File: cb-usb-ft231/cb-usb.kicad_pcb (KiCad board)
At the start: 2 copper layers, 25.4 x 55.8 mm, 26 parts, among them P1 CONN_01X14, P2 CONN_01X14, P3 CONN_01X05, SW1 SW_PUSH_SMALL, U1 ANTENNA, U2 FT231XS, U3 AP7365-33, U4 LY-SK10

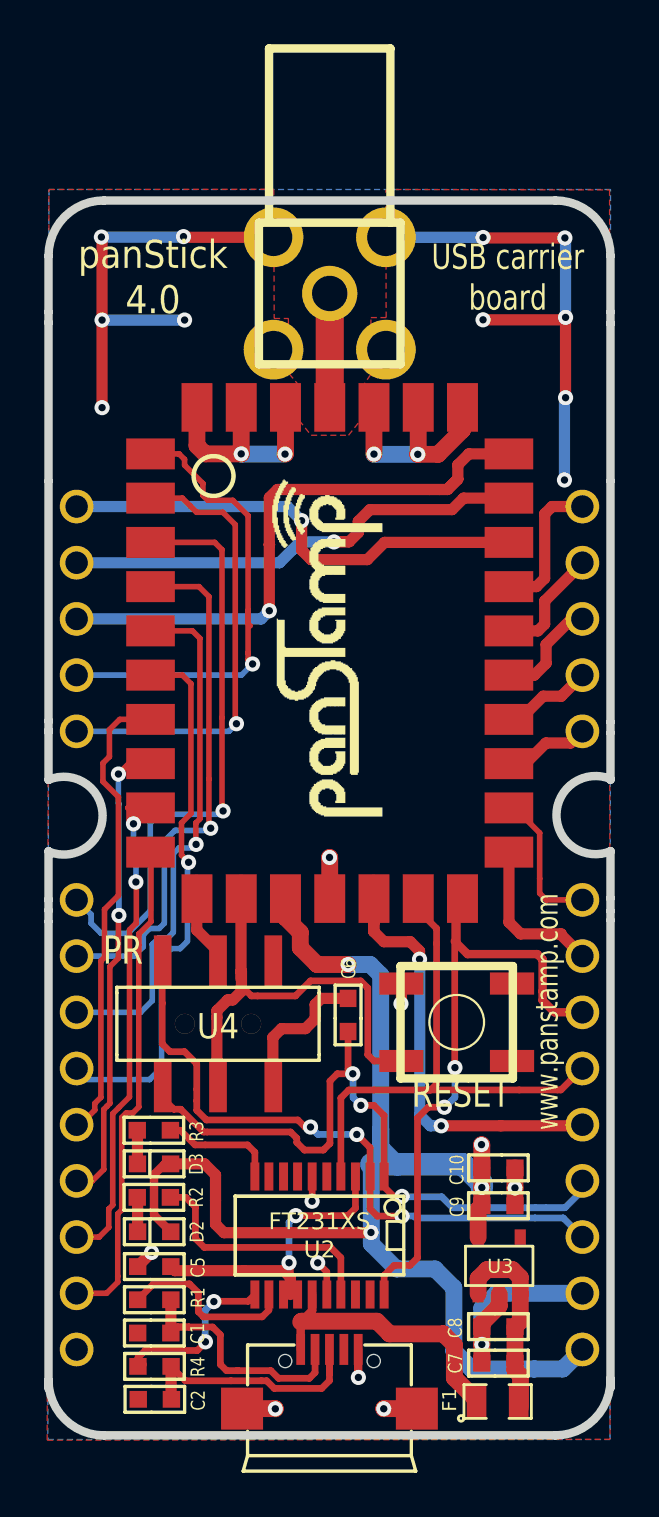
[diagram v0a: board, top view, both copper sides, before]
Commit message: Fiducials added to the PCB
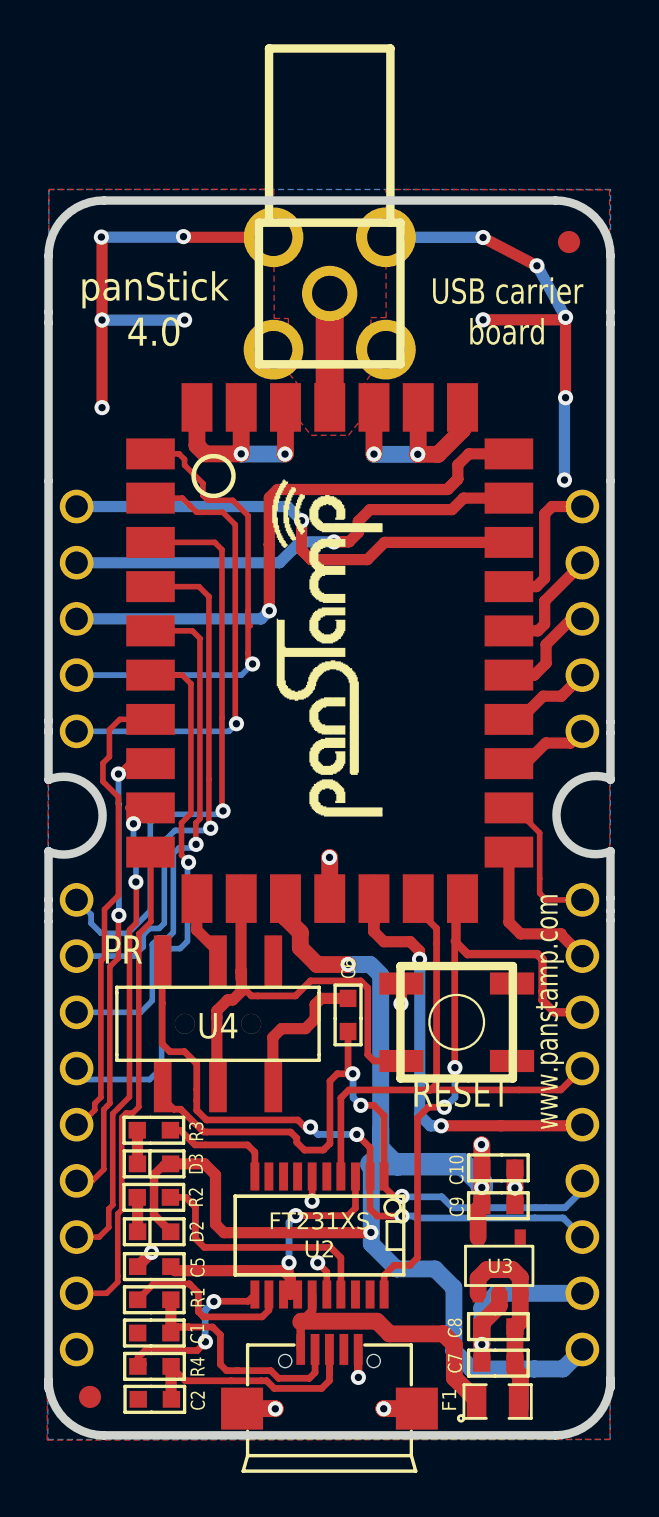
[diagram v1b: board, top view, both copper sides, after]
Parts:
- added fiducial: VAL**, mymods:fiducial, F.Cu at (164.1, 119.8)
- added fiducial: VAL**, mymods:fiducial, F.Cu at (185.8, 67.6)
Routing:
- net GND: track 86.3 -> 84.4 mm
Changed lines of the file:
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@@
-(kicad_pcb (version 4) (host pcbnew "(2014-jul-16 BZR unknown)-product")
+(kicad_pcb (version 4) (host pcbnew no-vcs-found-product)
   (general
     (links 86)
     (no_connects 0)
-    (area 162.059499 65.504799 187.850941 121.703321)
+    (area 154.644817 58.483079 195.375184 125.5577)
     (thickness 1.6002)
     (drawings 70)
     (tracks 695)
     (zones 0)
-    (modules 26)
+    (modules 28)
     (nets 51)
   )
@@
   )
   (setup
-    (last_trace_width 0.381)
+    (last_trace_width 0.1524)
     (user_trace_width 0.2032)
     (user_trace_width 0.254)
@@
     (visible_elements FFFFF7BF)
     (pcbplotparams
-      (layerselection 0x010f0_80000001)
+      (layerselection 0x00020_00000000)
       (usegerberextensions true)
       (excludeedgelayer true)
@@
     )
   )
+  (module mymods:fiducial (layer Front)
+    (at 164.125 119.775)
+    (fp_text reference fiducial (at 0 2.95) (layer F.SilkS) hide
+      (effects (font (thickness 0.3048)))
+    )
+    (fp_text value VAL** (at 0.925 3.625) (layer F.SilkS) hide
+      (effects (font (thickness 0.3048)))
+    )
+    (pad 1 smd circle (at 0 0) (size 1 1) (layers Front F.Mask)
+      (solder_mask_margin 0.5) (clearance 0.5))
+  )
+  (module mymods:fiducial (layer Front)
+    (at 185.775 67.575)
+    (fp_text reference fiducial (at 1.9 -3.65) (layer F.SilkS) hide
+      (effects (font (thickness 0.3048)))
+    )
+    (fp_text value VAL** (at 2.55 -4.1) (layer F.SilkS) hide
+      (effects (font (thickness 0.3048)))
+    )
+    (pad 1 smd circle (at 0 0) (size 1 1) (layers Front F.Mask)
+      (solder_mask_margin 0.5) (clearance 0.5))
+  )
   (gr_line (start 187.65012 68.19646) (end 187.64758 68.19646) (angle 90) (layer Edge.Cuts) (width 0.381))
   (gr_line (start 187.65012 70.73646) (end 187.65012 68.19646) (angle 90) (layer Edge.Cuts) (width 0.381))
@@
   (gr_line (start 187.65 118.93) (end 187.65 98.24) (angle 90) (layer Edge.Cuts) (width 0.381))
   (gr_line (start 162.25 98.3) (end 162.25 119.4) (angle 90) (layer Edge.Cuts) (width 0.381))
-  (gr_text "panStick\n4.0" (at 166.97 69.18) (layer F.SilkS)
+  (gr_text "panStick\n4.0" (at 167.025 70.65) (layer F.SilkS)
     (effects (font (size 1.27 1.143) (thickness 0.1524)))
   )
-  (gr_text "USB carrier\nboard" (at 183.01 69.18) (layer F.SilkS)
+  (gr_text "USB carrier\nboard" (at 182.975 70.75) (layer F.SilkS)
     (effects (font (size 1.143 0.889) (thickness 0.1524)))
   )
@@
   (segment (start 185.40962 105.90038) (end 186.38 104.93) (width 0.3048) (layer Front) (net 15))
   (segment (start 185.25744 105.90038) (end 185.40962 105.90038) (width 0.3048) (layer Front) (net 15))
+  (via (at 185.62 70.98038) (size 0.6858) (layers Front Back) (net 16))
+  (segment (start 181.89 67.37038) (end 181.91 67.39038) (width 0.508) (layer Front) (net 16))
+  (segment (start 181.91 67.39038) (end 184.325 68.65) (width 0.508) (layer Front) (net 16))
+  (via (at 184.325 68.65) (size 0.6858) (layers Front Back) (net 16))
+  (segment (start 184.325 68.65) (end 184.355 68.68) (width 0.508) (layer Back) (net 16))
+  (segment (start 184.355 68.68) (end 185.62 70.98038) (width 0.508) (layer Back) (net 16))
   (segment (start 178.89758 120.3024) (end 177.40846 120.3024) (width 0.762) (layer Front) (net 16))
   (via (at 177.40122 120.30964) (size 0.6858) (layers Front Back) (net 16))
@@
   (segment (start 168.38 67.36038) (end 168.35 67.33038) (width 0.508) (layer Front) (net 16))
   (segment (start 185.62 70.98038) (end 185.62 74.61038) (width 0.508) (layer Front) (net 16))
-  (via (at 185.57 78.33038) (size 0.6858) (layers Front Back) (net 16))
-  (segment (start 185.57 74.66038) (end 185.57 78.33038) (width 0.508) (layer Back) (net 16))
-  (segment (start 185.62 74.61038) (end 185.57 74.66038) (width 0.508) (layer Back) (net 16))
   (via (at 185.62 74.61038) (size 0.6858) (layers Front Back) (net 16))
+  (segment (start 185.62 74.61038) (end 185.57 74.66038) (width 0.508) (layer Back) (net 16))
+  (segment (start 185.57 74.66038) (end 185.57 78.33038) (width 0.508) (layer Back) (net 16))
+  (via (at 185.57 78.33038) (size 0.6858) (layers Front Back) (net 16))
   (segment (start 177.5 67.36038) (end 181.88 67.36038) (width 0.508) (layer Back) (net 16))
   (segment (start 181.89 71.09038) (end 181.89 71.13038) (width 0.508) (layer Back) (net 16))
-  (via (at 181.89 71.09038) (size 0.6858) (layers Front Back) (net 16))
-  (segment (start 185.51 71.09038) (end 181.89 71.09038) (width 0.508) (layer Front) (net 16))
   (segment (start 185.62 70.98038) (end 185.51 71.09038) (width 0.508) (layer Front) (net 16))
-  (via (at 185.62 70.98038) (size 0.6858) (layers Front Back) (net 16))
-  (segment (start 185.62 67.42038) (end 185.62 70.98038) (width 0.508) (layer Back) (net 16))
-  (segment (start 185.59 67.39038) (end 185.62 67.42038) (width 0.508) (layer Back) (net 16))
-  (via (at 185.59 67.39038) (size 0.6858) (layers Front Back) (net 16))
-  (segment (start 181.91 67.39038) (end 185.59 67.39038) (width 0.508) (layer Front) (net 16))
-  (segment (start 181.89 67.37038) (end 181.91 67.39038) (width 0.508) (layer Front) (net 16))
+  (segment (start 185.51 71.09038) (end 181.89 71.09038) (width 0.508) (layer Front) (net 16))
+  (via (at 181.89 71.09038) (size 0.6858) (layers Front Back) (net 16))
   (via (at 181.89 67.37038) (size 0.6858) (layers Front Back) (net 16))
   (segment (start 181.88 67.36038) (end 181.89 67.37038) (width 0.508) (layer Back) (net 16))

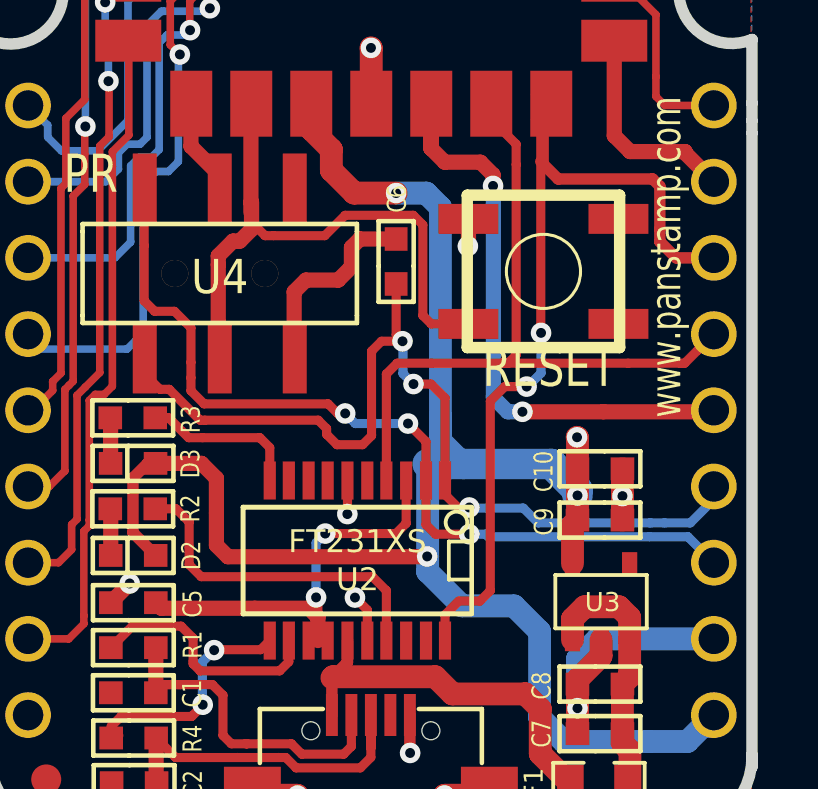
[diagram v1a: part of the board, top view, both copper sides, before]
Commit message: RESET and TEST lines forwarded to the right lines
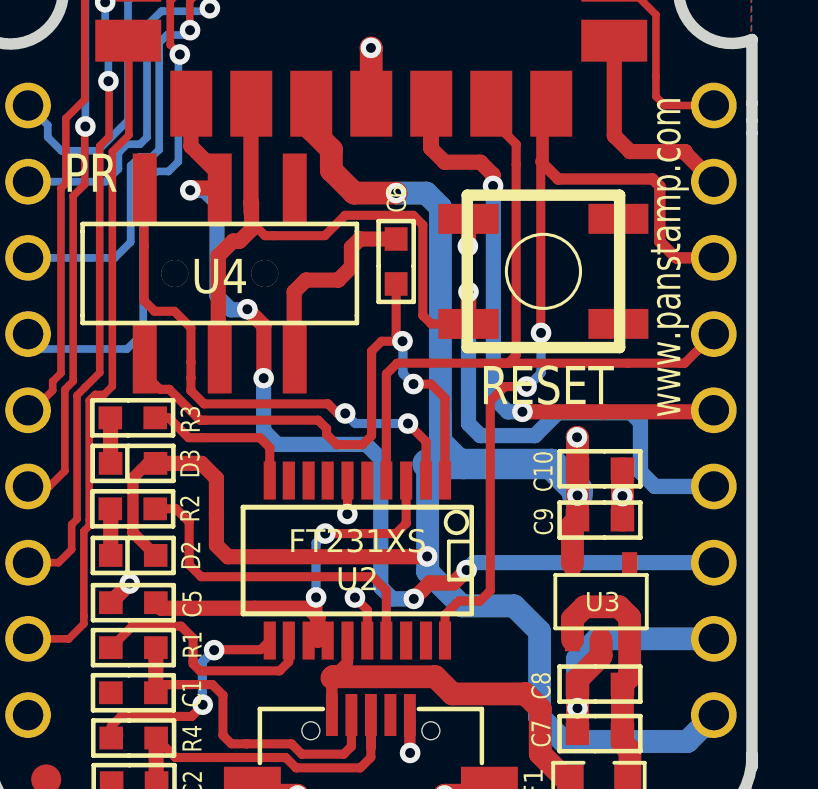
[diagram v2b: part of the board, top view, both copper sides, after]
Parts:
- C7: value 4.7u -> 10u
- PS1: footprint mysmd:PANSTAMP_2 -> PANSTAMP_2
- U2: footprint libcms:SSOP20 -> SSOP20
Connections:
- P2 pad 11: /RESET -> /NRG_RESET
- P2 pad 12: /TEST -> /NRG_TEST
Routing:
- net /NRG_TEST: track 4.39 -> 35.4 mm, vias 0 -> 5
- net /NRG_RESET: track 23.1 -> 39.2 mm, vias 0 -> 1
- net /TEST: track 30.7 -> 18.1 mm, vias 3 -> 2
- net /RESET: track 31.4 -> 21.3 mm, vias 3 -> 2
